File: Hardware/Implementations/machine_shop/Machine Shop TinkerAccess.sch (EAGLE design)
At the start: 39 parts, among them J1 TB_2X1_TE_CONN_ED555_2DS, J10 HDR_4X1_2.54MM_LOCKING_RA, J2 TB_2X1_TE_CONN_ED555_2DS, J3 TB_2X1_TE_CONN_ED555_2DS, J4 TB_2X1_TE_CONN_ED555_2DS, J5 TB_2X1_TE_CONN_ED555_2DS, J6 TB_2X1_TE_CONN_ED555_2DS, J7 TB_2X1_TE_CONN_ED555_2DS, J8 HDR_4X1_2.54MM_LOCKING_RA, J9 HDR_4X1_2.54MM_LOCKING_RA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

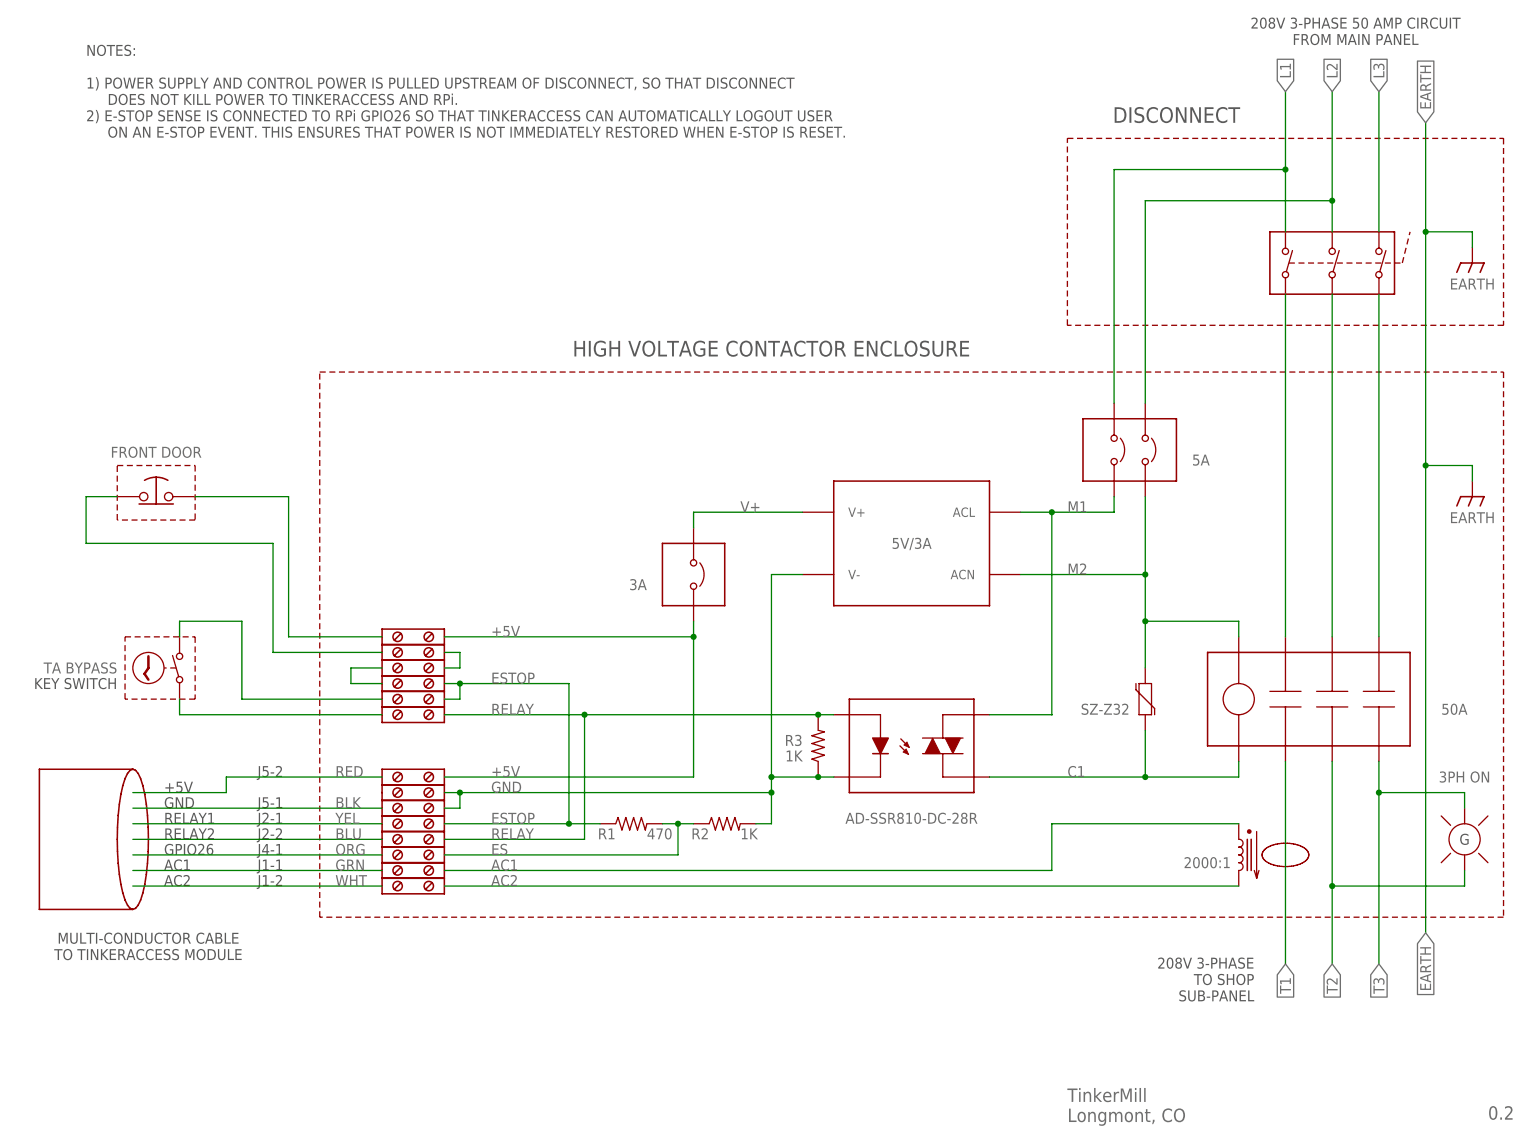
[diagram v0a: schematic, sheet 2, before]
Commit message: Modified schematic to connect RPi power supply to load side of disconnect.
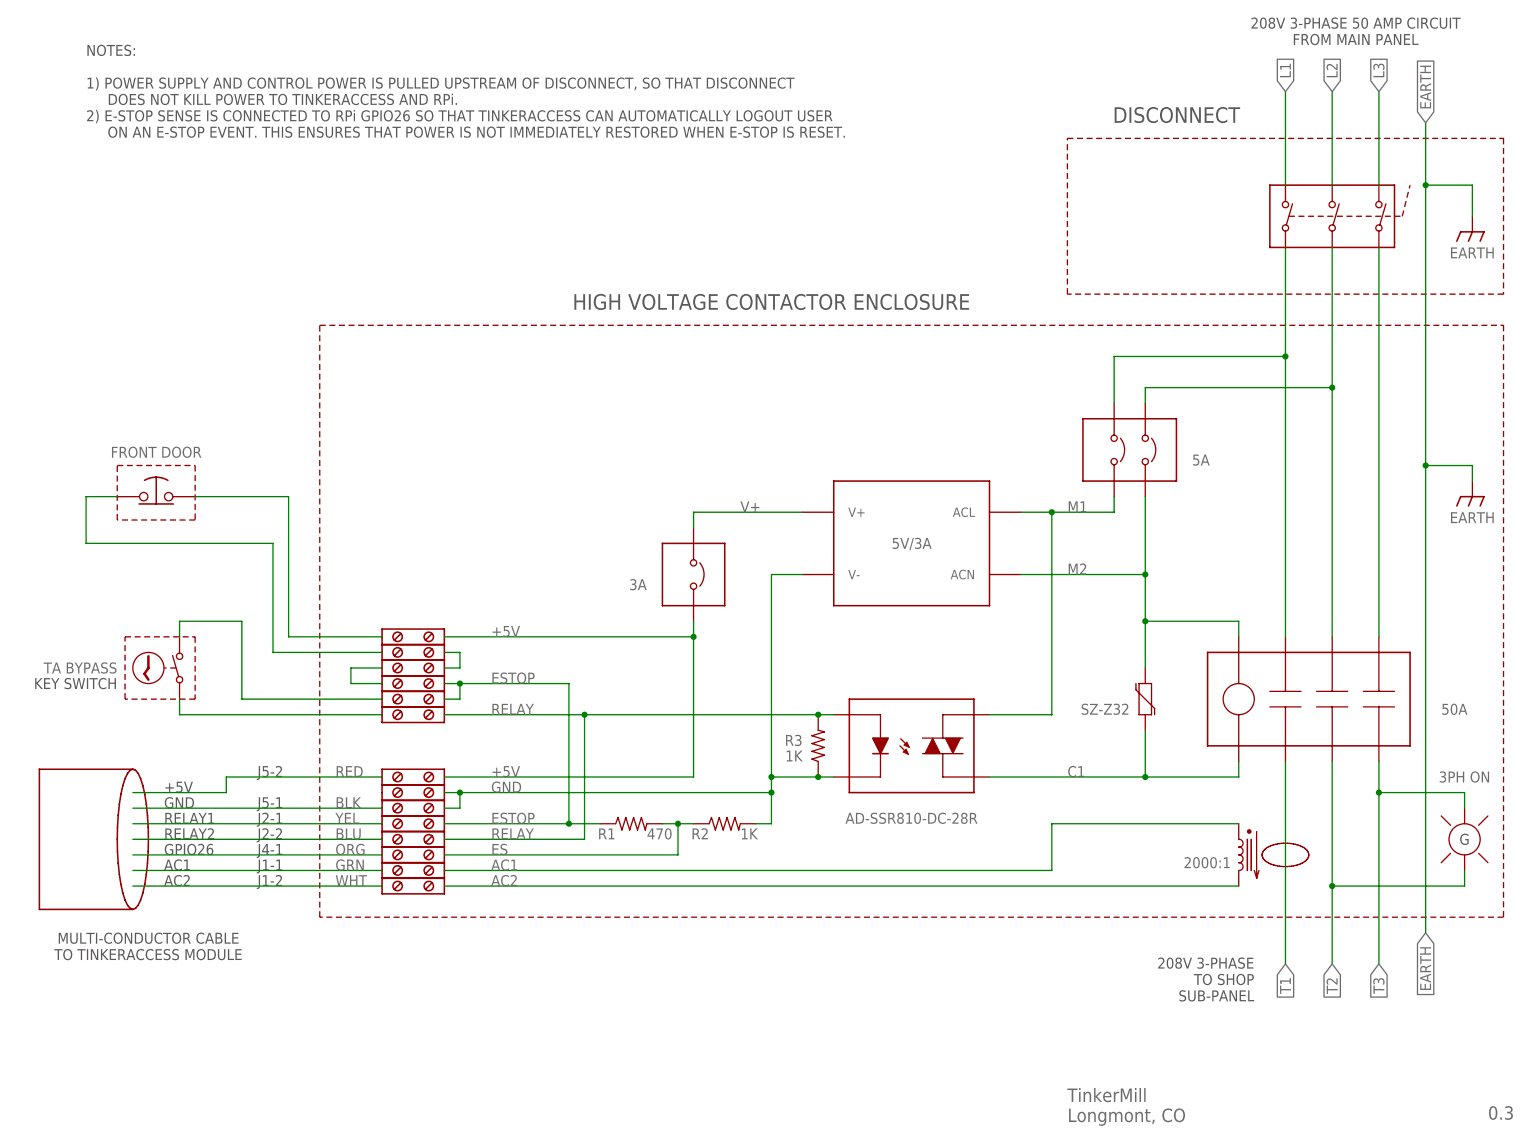
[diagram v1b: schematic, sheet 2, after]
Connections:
- net L1: no longer CB1.L1
- net L2: no longer CB1.L2
- net S1: now also CB1.L1
- net S2: now also CB1.L2
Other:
- note added: "0.3"
- note removed: "0.2"
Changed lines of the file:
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@@
 <?xml version="1.0" encoding="utf-8"?>
 <!DOCTYPE eagle SYSTEM "eagle.dtd">
-<eagle version="9.5.1">
+<eagle version="9.6.1">
 <drawing>
 <settings>
@@
 <text x="175.26" y="12.7" size="2.1844" layer="95" align="top-left">TinkerMill
 Longmont, CO</text>
-<text x="243.84" y="7.62" size="2.1844" layer="95">0.2</text>
+<text x="243.84" y="7.62" size="2.1844" layer="95">0.3</text>
 <wire x1="46.99" y1="53.34" x2="64.77" y2="53.34" width="0.254" layer="94"/>
 <wire x1="64.77" y1="53.34" x2="64.77" y2="35.56" width="0.254" layer="94"/>
@@
 <text x="175.26" y="12.7" size="2.1844" layer="95" align="top-left">TinkerMill
 Longmont, CO</text>
-<text x="243.84" y="7.62" size="2.1844" layer="95">0.2</text>
-<text x="127" y="132.08" size="2.54" layer="97" align="bottom-center">HIGH VOLTAGE CONTACTOR ENCLOSURE</text>
+<text x="243.84" y="7.62" size="2.1844" layer="95">0.3</text>
+<text x="127" y="139.7" size="2.54" layer="97" align="bottom-center">HIGH VOLTAGE CONTACTOR ENCLOSURE</text>
 <wire x1="21.59" y1="86.36" x2="33.02" y2="86.36" width="0.1524" layer="94" style="shortdash"/>
 <wire x1="33.02" y1="86.36" x2="33.02" y2="76.2" width="0.1524" layer="94" style="shortdash"/>
@@
 <wire x1="20.32" y1="105.41" x2="20.32" y2="114.3" width="0.1524" layer="94" style="shortdash"/>
 <wire x1="246.38" y1="40.64" x2="53.34" y2="40.64" width="0.1524" layer="94" style="shortdash"/>
-<wire x1="53.34" y1="40.64" x2="53.34" y2="129.54" width="0.1524" layer="94" style="shortdash"/>
-<wire x1="53.34" y1="129.54" x2="246.38" y2="129.54" width="0.1524" layer="94" style="shortdash"/>
-<wire x1="246.38" y1="129.54" x2="246.38" y2="40.64" width="0.1524" layer="94" style="shortdash"/>
+<wire x1="53.34" y1="40.64" x2="53.34" y2="137.16" width="0.1524" layer="94" style="shortdash"/>
+<wire x1="53.34" y1="137.16" x2="246.38" y2="137.16" width="0.1524" layer="94" style="shortdash"/>
+<wire x1="246.38" y1="137.16" x2="246.38" y2="40.64" width="0.1524" layer="94" style="shortdash"/>
 <wire x1="22.86" y1="64.77" x2="7.62" y2="64.77" width="0.254" layer="94"/>
 <wire x1="7.62" y1="64.77" x2="7.62" y2="41.91" width="0.254" layer="94"/>
@@
 <text x="43.18" y="45.72" size="1.778" layer="97">J1-2</text>
 <wire x1="175.26" y1="167.64" x2="246.38" y2="167.64" width="0.1524" layer="94" style="shortdash"/>
-<wire x1="246.38" y1="167.64" x2="246.38" y2="137.16" width="0.1524" layer="94" style="shortdash"/>
-<wire x1="246.38" y1="137.16" x2="175.26" y2="137.16" width="0.1524" layer="94" style="shortdash"/>
-<wire x1="175.26" y1="137.16" x2="175.26" y2="167.64" width="0.1524" layer="94" style="shortdash"/>
+<wire x1="246.38" y1="167.64" x2="246.38" y2="142.24" width="0.1524" layer="94" style="shortdash"/>
+<wire x1="246.38" y1="142.24" x2="175.26" y2="142.24" width="0.1524" layer="94" style="shortdash"/>
+<wire x1="175.26" y1="142.24" x2="175.26" y2="167.64" width="0.1524" layer="94" style="shortdash"/>
 <text x="193.04" y="170.18" size="2.54" layer="97" align="bottom-center">DISCONNECT</text>
 <wire x1="25.4" y1="53.34" x2="25.3614125" y2="55.3248" width="0.254" layer="94"/>
@@
 <attribute name="VALUE" x="121.92" y="53.34" size="1.778" layer="96"/>
 </instance>
-<instance part="SW2" gate="G$1" x="218.44" y="147.32" smashed="yes"/>
-<instance part="SUPPLY2" gate="G$1" x="241.3" y="149.86" smashed="yes">
-<attribute name="VALUE" x="241.3" y="144.78" size="1.778" layer="96" align="top-center"/>
+<instance part="SW2" gate="G$1" x="218.44" y="154.94" smashed="yes"/>
+<instance part="SUPPLY2" gate="G$1" x="241.3" y="154.94" smashed="yes">
+<attribute name="VALUE" x="241.3" y="149.86" size="1.778" layer="96" align="top-center"/>
 </instance>
 <instance part="LP1" gate="G$1" x="240.03" y="53.34" smashed="yes" rot="R90">
@@
 <segment>
 <pinref part="K1" gate="G$1" pin="L1"/>
-<wire x1="210.82" y1="86.36" x2="210.82" y2="142.24" width="0.1524" layer="91"/>
+<wire x1="210.82" y1="86.36" x2="210.82" y2="132.08" width="0.1524" layer="91"/>
 <pinref part="SW2" gate="G$1" pin="T1"/>
+<pinref part="CB1" gate="G$1" pin="L1"/>
+<wire x1="210.82" y1="132.08" x2="210.82" y2="149.86" width="0.1524" layer="91"/>
+<wire x1="182.88" y1="124.46" x2="182.88" y2="132.08" width="0.1524" layer="91"/>
+<wire x1="182.88" y1="132.08" x2="210.82" y2="132.08" width="0.1524" layer="91"/>
+<junction x="210.82" y="132.08"/>
 </segment>
 </net>
@@
 <segment>
 <pinref part="K1" gate="G$1" pin="L2"/>
-<wire x1="218.44" y1="86.36" x2="218.44" y2="142.24" width="0.1524" layer="91"/>
+<wire x1="218.44" y1="86.36" x2="218.44" y2="127" width="0.1524" layer="91"/>
 <pinref part="SW2" gate="G$1" pin="T2"/>
+<pinref part="CB1" gate="G$1" pin="L2"/>
+<wire x1="218.44" y1="127" x2="218.44" y2="149.86" width="0.1524" layer="91"/>
+<wire x1="187.96" y1="124.46" x2="187.96" y2="127" width="0.1524" layer="91"/>
+<wire x1="187.96" y1="127" x2="218.44" y2="127" width="0.1524" layer="91"/>
+<junction x="218.44" y="127"/>
 </segment>
 </net>
@@
 <segment>
 <pinref part="K1" gate="G$1" pin="L3"/>
-<wire x1="226.06" y1="86.36" x2="226.06" y2="142.24" width="0.1524" layer="91"/>
+<wire x1="226.06" y1="86.36" x2="226.06" y2="149.86" width="0.1524" layer="91"/>
 <pinref part="SW2" gate="G$1" pin="T3"/>
 </segment>
@@
 <segment>
 <pinref part="SUPPLY2" gate="G$1" pin="EARTH"/>
-<wire x1="241.3" y1="149.86" x2="241.3" y2="152.4" width="0.1524" layer="91"/>
+<wire x1="241.3" y1="154.94" x2="241.3" y2="160.02" width="0.1524" layer="91"/>
 <pinref part="SUPPLY1" gate="G$1" pin="EARTH"/>
 <wire x1="241.3" y1="111.76" x2="241.3" y2="114.3" width="0.1524" layer="91"/>
 <wire x1="241.3" y1="114.3" x2="233.68" y2="114.3" width="0.1524" layer="91"/>
-<wire x1="233.68" y1="114.3" x2="233.68" y2="152.4" width="0.1524" layer="91"/>
+<wire x1="233.68" y1="114.3" x2="233.68" y2="160.02" width="0.1524" layer="91"/>
 <label x="233.68" y="170.18" size="1.778" layer="95" rot="R90" xref="yes"/>
-<wire x1="233.68" y1="152.4" x2="233.68" y2="170.18" width="0.1524" layer="91"/>
-<wire x1="241.3" y1="152.4" x2="233.68" y2="152.4" width="0.1524" layer="91"/>
-<junction x="233.68" y="152.4"/>
+<wire x1="233.68" y1="160.02" x2="233.68" y2="170.18" width="0.1524" layer="91"/>
+<wire x1="241.3" y1="160.02" x2="233.68" y2="160.02" width="0.1524" layer="91"/>
+<junction x="233.68" y="160.02"/>
 <junction x="233.68" y="114.3"/>
 <wire x1="233.68" y1="114.3" x2="233.68" y2="38.1" width="0.1524" layer="91"/>
@@
 <segment>
 <pinref part="SW2" gate="G$1" pin="L1"/>
-<wire x1="210.82" y1="152.4" x2="210.82" y2="162.56" width="0.1524" layer="91"/>
 <label x="210.82" y="175.26" size="1.778" layer="95" rot="R90" xref="yes"/>
-<pinref part="CB1" gate="G$1" pin="L1"/>
-<wire x1="210.82" y1="162.56" x2="210.82" y2="175.26" width="0.1524" layer="91"/>
-<wire x1="182.88" y1="124.46" x2="182.88" y2="162.56" width="0.1524" layer="91"/>
-<wire x1="182.88" y1="162.56" x2="210.82" y2="162.56" width="0.1524" layer="91"/>
-<junction x="210.82" y="162.56"/>
+<wire x1="210.82" y1="160.02" x2="210.82" y2="175.26" width="0.1524" layer="91"/>
 </segment>
 </net>
@@
 <segment>
 <pinref part="SW2" gate="G$1" pin="L2"/>
-<wire x1="218.44" y1="152.4" x2="218.44" y2="157.48" width="0.1524" layer="91"/>
 <label x="218.44" y="175.26" size="1.778" layer="95" rot="R90" xref="yes"/>
-<pinref part="CB1" gate="G$1" pin="L2"/>
-<wire x1="218.44" y1="157.48" x2="218.44" y2="175.26" width="0.1524" layer="91"/>
-<wire x1="187.96" y1="124.46" x2="187.96" y2="157.48" width="0.1524" layer="91"/>
-<wire x1="187.96" y1="157.48" x2="218.44" y2="157.48" width="0.1524" layer="91"/>
-<junction x="218.44" y="157.48"/>
+<wire x1="218.44" y1="160.02" x2="218.44" y2="175.26" width="0.1524" layer="91"/>
 </segment>
 </net>
@@
 <segment>
 <pinref part="SW2" gate="G$1" pin="L3"/>
-<wire x1="226.06" y1="152.4" x2="226.06" y2="175.26" width="0.1524" layer="91"/>
+<wire x1="226.06" y1="160.02" x2="226.06" y2="175.26" width="0.1524" layer="91"/>
 <label x="226.06" y="175.26" size="1.778" layer="95" rot="R90" xref="yes"/>
 </segment>
@@
 <text x="175.26" y="12.7" size="2.1844" layer="95" align="top-left">TinkerMill
 Longmont, CO</text>
-<text x="243.84" y="7.62" size="2.1844" layer="95">0.2</text>
+<text x="243.84" y="7.62" size="2.1844" layer="95">0.3</text>
 <text x="95.25" y="114.3" size="1.778" layer="97" align="center-left">+5V</text>
 <text x="95.25" y="111.76" size="1.778" layer="97" align="center-left">GND</text>

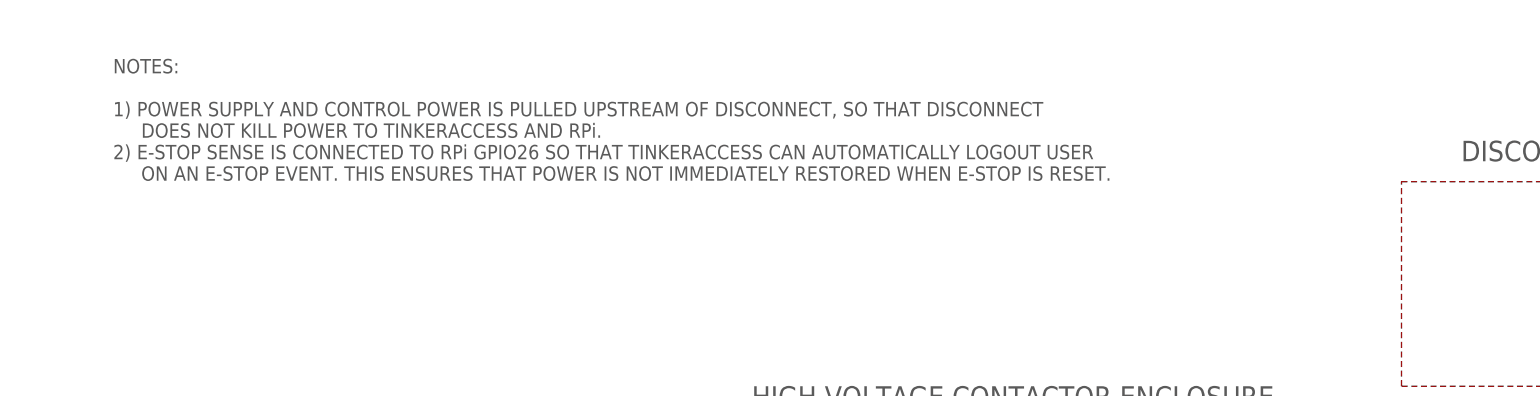
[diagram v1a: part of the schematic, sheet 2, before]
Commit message: Cleaned up schematic notes
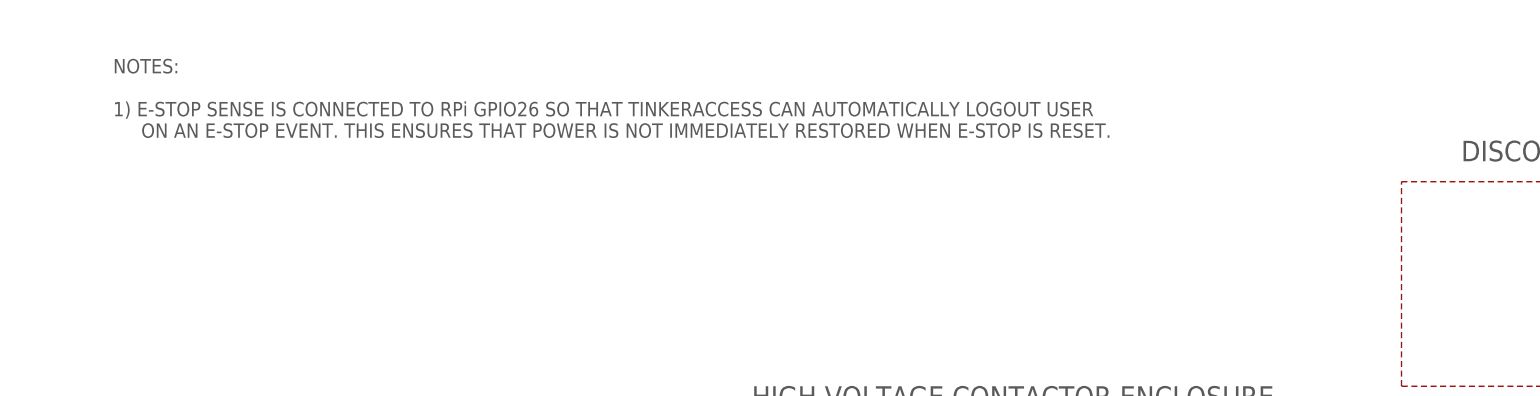
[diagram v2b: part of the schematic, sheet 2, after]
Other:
- note added: "NOTES: 1) E-STOP SENSE IS CONNECTED TO RPi GPIO26 SO THAT TINKERACCESS CAN AUTOMATICALLY LOGOUT USER ON AN E-STOP EVENT. THIS ENSURES THAT POWER IS NOT IMMEDIATELY RESTORED WHEN E-STOP IS RESET."
- note removed: "NOTES: 1) POWER SUPPLY AND CONTROL POWER IS PULLED UPSTREAM OF DISCONNECT, SO THAT DISCONNECT DOES NOT KILL POWER TO TINKERACCESS AND RPi. 2) E-STOP SENSE IS CONNECTED TO RPi GPIO26 SO THAT TINKERACCESS CAN AUTOMATICALLY LOGOUT USER ON AN E-STOP EVENT. THIS ENSURES THAT POWER IS NOT IMMEDIATELY RESTORED WHEN E-STOP IS RESET."
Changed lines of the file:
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@@
 <wire x1="25.3614125" y1="51.3552" x2="25.4" y2="53.34" width="0.254" layer="94"/>
 <text x="15.24" y="182.88" size="1.778" layer="97" align="top-left">NOTES:
-1) POWER SUPPLY AND CONTROL POWER IS PULLED UPSTREAM OF DISCONNECT, SO THAT DISCONNECT
-     DOES NOT KILL POWER TO TINKERACCESS AND RPi.
-2) E-STOP SENSE IS CONNECTED TO RPi GPIO26 SO THAT TINKERACCESS CAN AUTOMATICALLY LOGOUT USER
+1) E-STOP SENSE IS CONNECTED TO RPi GPIO26 SO THAT TINKERACCESS CAN AUTOMATICALLY LOGOUT USER
      ON AN E-STOP EVENT. THIS ENSURES THAT POWER IS NOT IMMEDIATELY RESTORED WHEN E-STOP IS RESET.</text>
 <text x="240.03" y="53.34" size="1.778" layer="97" align="center">G</text>

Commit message: Updates to machine shop TA schematic.
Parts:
- added J11: HDR_4X1_2.54MM_LOCKING_RA, TMF_Connectors:HDR_4X1_2.54MM_LOCKING_RA
- added TB4: TERMINAL_BLOCK, TMF_Schematic_Only:TERMINAL_BLOCK
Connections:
- removed net N$11: J10.4, J8.4
- removed net N$12: J10.3, J8.3
- removed net N$13: J10.2, J8.2
- removed net N$14: J10.1, J8.1
- removed net ORG: J4.1, TB7.A
- removed net YEL: J2.1, TB5.A
- new net BRN: J1.1, TB9.A
- new net N$17: J11.1, J9.1
- new net N$18: J11.2, J9.2
- new net N$19: J11.3, J9.3
- new net N$20: J11.4, J9.4
- new net SHLD: TB3.A
- new net ZBLK: J5.1, TB2.A
- new net ZRED: J5.2, TB1.A
- net BLK: now also TB4.A; no longer J5.1, TB3.A
- net BLU: now also J1.2, TB10.A; no longer J2.2, TB6.A
- net GRN: now also J2.2, TB6.A; no longer J1.1, TB9.A
- net RED: now also J4.1, TB7.A; no longer J5.2, TB1.A
- net WHT: now also J2.1, TB5.A; no longer J1.2, TB10.A
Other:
- note added: "0.4"
- note added: "ENTRY DOOR"
- note added: "SHIELD"
- note added: "SPARE"
- note removed: "0.3"
- note removed: "FRONT DOOR"
- note removed: "GPIO19"
